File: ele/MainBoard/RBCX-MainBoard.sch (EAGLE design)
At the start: 340 parts, among them IC1 DRV8833PWP, IC10 INA180A4, IC11 AMS1117-3.3, IC2 INA180A4, IC3 INA180A4, IC4 DRV8833PWP, IC5 INA180A4, IC6 INA180A4, IC7 INA180A4, IC8 INA180A4, IC9 INA180A4, Q1 CHOOSE_ME, Q2 CHOOSE_ME, Q3 CHOOSE_ME, Q4 CHOOSE_ME, Q5 CHOOSE_ME, Q6 CHOOSE_ME, Q7 CHOOSE_ME, Q8 CHOOSE_ME, Q9 CHOOSE_ME, U1 STM32F103VCT6, X0 POWER_IN, X1 M3B, X2 M4B, X3 M3B, X4 M4B, X5 POWER_OUT, Y1 3215_2P, Y2 5032/2P

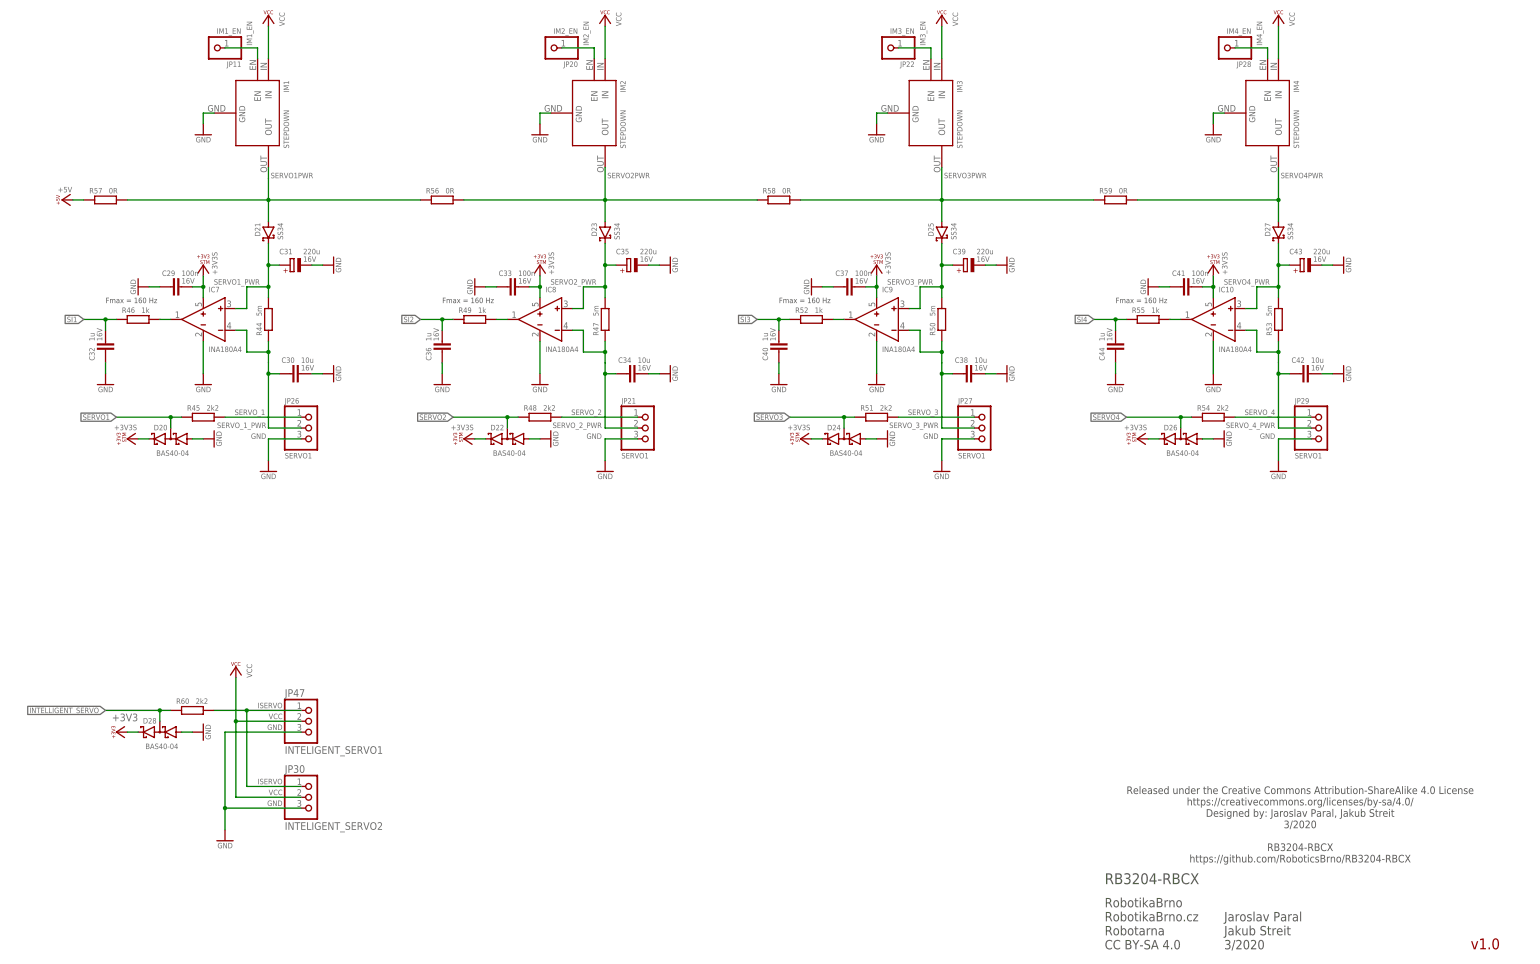
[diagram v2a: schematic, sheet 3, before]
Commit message: MainBoardSCH: Add bulk capacitor to stepdowns and drivers
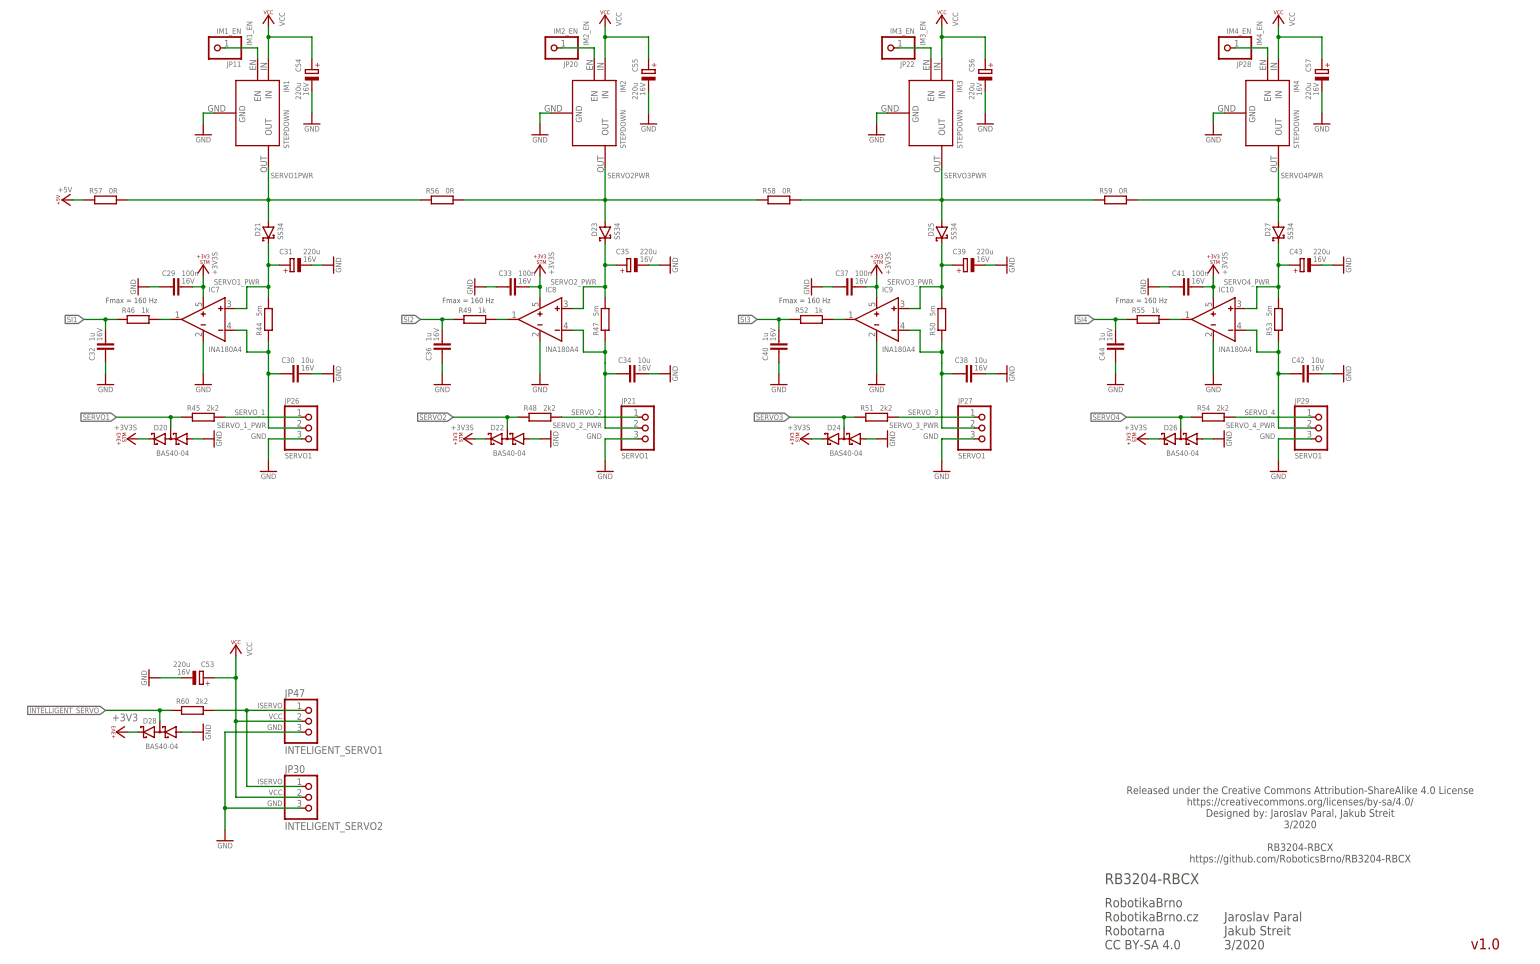
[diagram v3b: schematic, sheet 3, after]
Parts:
- added C51, C52, C53, C54, C55, C56, C57, C58: 220u, rcl_upravena:CPOL-EU153CLV-1010
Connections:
- net GND: now also C51.-, C52.-, C53.-, C54.-, C55.-, C56.-, C57.-, C58.-
- net VCC: now also C51.+, C52.+, C53.+, C54.+, C55.+, C56.+, C57.+, C58.+

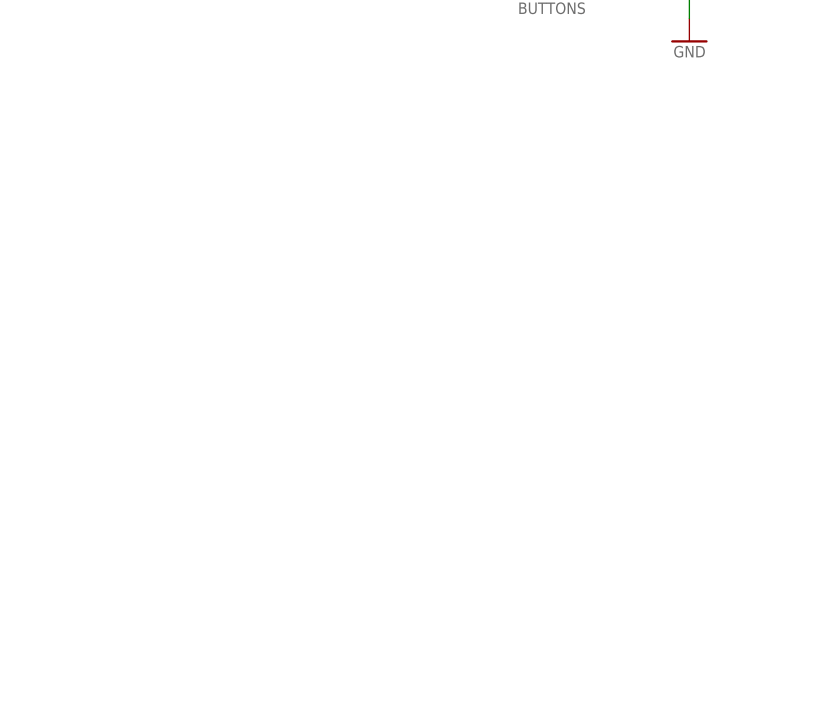
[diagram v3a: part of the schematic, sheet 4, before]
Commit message: MainBoardSCH: Add buzzer
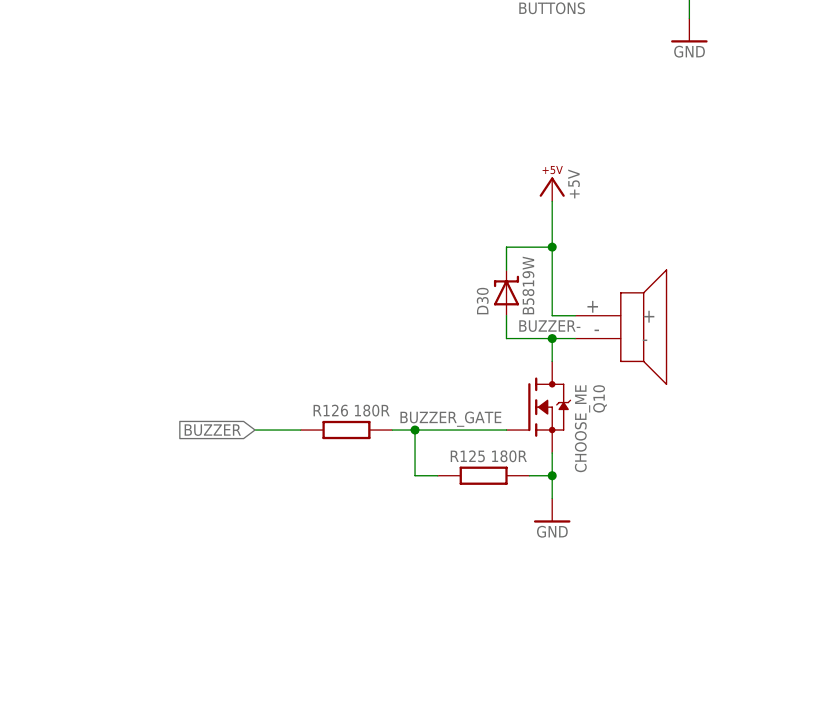
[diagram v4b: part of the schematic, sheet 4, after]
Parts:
- added D30: B5819W, diode:SHOTTKY-SOD123
- added Q10: CHOOSE_ME, transistors:N-MOSFET-SOT323-GSD
- added R125, R126: 180R, rcl_upravena:R-EU_R0603
- added U$1: PIEZO, piezo:PIEZO
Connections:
- new net BUZZER-: D30.A, Q10.D, U$1.-
- new net BUZZER_GATE: Q10.G, R125.1, R126.2
- net +5V: now also D30.C, U$1.+
- net BUZZER: now also R126.1
- net GND: now also Q10.S, R125.2
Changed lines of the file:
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@@
 </part>
 <part name="GND155" library="Supply" deviceset="GND" device=""/>
+<part name="U$1" library="piezo" deviceset="PIEZO" device=""/>
+<part name="Q10" library="transistors" deviceset="N-MOSFET" device="-SOT323-GSD" value="CHOOSE_ME"/>
+<part name="GND156" library="Supply" deviceset="GND" device=""/>
+<part name="R125" library="rcl_upravena" deviceset="R-EU_" device="R0603" value="180R"/>
+<part name="R126" library="rcl_upravena" deviceset="R-EU_" device="R0603" value="180R"/>
+<part name="P+37" library="Supply" deviceset="+5V" device=""/>
+<part name="D30" library="diode" deviceset="SHOTTKY" device="-SOD123" value="B5819W">
+<attribute name="DESCRIPTION" value="40V 1A 600mV @ 1A SOD-123 Schottky Barrier Diodes (SBD) RoHS"/>
+<attribute name="EXTENDED" value="NO"/>
+<attribute name="LCSC_ID" value="C305445"/>
+<attribute name="MF" value="Foshan Blue Rocket Elec"/>
+<attribute name="MF_ID" value="B5819W"/>
+<attribute name="PACKAGE" value="SOD-123"/>
+<attribute name="PADS" value="2"/>
+<attribute name="PRICE_100PLUS" value="$0.0176"/>
+<attribute name="PRICE_1PLUS" value="$0.0342"/>
+<attribute name="PRICE_DATE" value="17.03.2020"/>
+</part>
 </parts>
 <sheets>
@@
 <attribute name="VALUE" x="214.122" y="65.024" size="1.27" layer="96"/>
 </instance>
+<instance part="U$1" gate="G$1" x="236.22" y="142.24" smashed="yes"/>
+<instance part="Q10" gate="G$1" x="226.06" y="137.16" smashed="yes">
+<attribute name="VALUE" x="231.14" y="139.7" size="1.27" layer="96" rot="R270"/>
+<attribute name="NAME" x="233.172" y="139.7" size="1.27" layer="95" rot="R270"/>
+</instance>
+<instance part="GND156" gate="1" x="228.6" y="124.46" smashed="yes">
+<attribute name="VALUE" x="226.822" y="122.682" size="1.27" layer="96"/>
+</instance>
+<instance part="R125" gate="G$1" x="220.98" y="129.54" smashed="yes">
+<attribute name="NAME" x="217.17" y="131.064" size="1.27" layer="95"/>
+<attribute name="VALUE" x="221.742" y="131.064" size="1.27" layer="96"/>
+</instance>
+<instance part="R126" gate="G$1" x="205.74" y="134.62" smashed="yes">
+<attribute name="NAME" x="201.93" y="136.144" size="1.27" layer="95"/>
+<attribute name="VALUE" x="206.502" y="136.144" size="1.27" layer="96"/>
+</instance>
+<instance part="P+37" gate="1" x="228.6" y="162.56" smashed="yes" rot="MR0">
+<attribute name="VALUE" x="230.378" y="163.576" size="1.27" layer="96" rot="R270"/>
+</instance>
+<instance part="D30" gate="G$1" x="223.52" y="149.86" smashed="yes" rot="R90">
+<attribute name="NAME" x="221.5134" y="147.32" size="1.27" layer="95" rot="R90"/>
+<attribute name="VALUE" x="226.5934" y="147.32" size="1.27" layer="96" rot="R90"/>
+<attribute name="EXTENDED" x="223.52" y="149.86" size="1.27" layer="96" rot="R90" display="off"/>
+<attribute name="LCSC_ID" x="223.52" y="149.86" size="1.27" layer="96" rot="R90" display="off"/>
+<attribute name="MF" x="223.52" y="149.86" size="1.27" layer="96" rot="R90" display="off"/>
+<attribute name="MF_ID" x="223.52" y="149.86" size="1.27" layer="96" rot="R90" display="off"/>
+<attribute name="PACKAGE" x="223.52" y="149.86" size="1.27" layer="96" rot="R90" display="off"/>
+<attribute name="PADS" x="223.52" y="149.86" size="1.27" layer="96" rot="R90" display="off"/>
+<attribute name="PRICE_100PLUS" x="223.52" y="149.86" size="1.27" layer="96" rot="R90" display="off"/>
+<attribute name="PRICE_1PLUS" x="223.52" y="149.86" size="1.27" layer="96" rot="R90" display="off"/>
+<attribute name="PRICE_DATE" x="223.52" y="149.86" size="1.27" layer="96" rot="R90" display="off"/>
+<attribute name="DESCRIPTION" x="223.52" y="149.86" size="1.27" layer="96" rot="R90" display="off"/>
+</instance>
 </instances>
 <busses>
@@
 <junction x="243.84" y="55.88"/>
 </segment>
+<segment>
+<pinref part="Q10" gate="G$1" pin="S"/>
+<pinref part="GND156" gate="1" pin="GND"/>
+<wire x1="228.6" y1="132.08" x2="228.6" y2="129.54" width="0.1524" layer="91"/>
+<pinref part="R125" gate="G$1" pin="2"/>
+<wire x1="228.6" y1="129.54" x2="228.6" y2="127" width="0.1524" layer="91"/>
+<wire x1="226.06" y1="129.54" x2="228.6" y2="129.54" width="0.1524" layer="91"/>
+<junction x="228.6" y="129.54"/>
+</segment>
 </net>
 <net name="SERVO1" class="0">
@@
 <pinref part="U1" gate="G$1" pin="PA8"/>
 </segment>
+<segment>
+<pinref part="R126" gate="G$1" pin="1"/>
+<wire x1="200.66" y1="134.62" x2="195.58" y2="134.62" width="0.1524" layer="91"/>
+<label x="195.58" y="134.62" size="1.27" layer="95" rot="MR0" xref="yes"/>
+</segment>
 </net>
 <net name="DEBUG_TX" class="0">
@@
 </segment>
 </net>
+<net name="BUZZER-" class="0">
+<segment>
+<pinref part="U$1" gate="G$1" pin="-"/>
+<wire x1="231.14" y1="144.78" x2="228.6" y2="144.78" width="0.1524" layer="91"/>
+<pinref part="Q10" gate="G$1" pin="D"/>
+<wire x1="228.6" y1="144.78" x2="228.6" y2="142.24" width="0.1524" layer="91"/>
+<pinref part="D30" gate="G$1" pin="A"/>
+<wire x1="223.52" y1="147.32" x2="223.52" y2="144.78" width="0.1524" layer="91"/>
+<wire x1="223.52" y1="144.78" x2="228.6" y2="144.78" width="0.1524" layer="91"/>
+<junction x="228.6" y="144.78"/>
+<label x="224.79" y="145.542" size="1.27" layer="95"/>
+</segment>
+</net>
+<net name="+5V" class="0">
+<segment>
+<pinref part="U$1" gate="G$1" pin="+"/>
+<pinref part="P+37" gate="1" pin="+5V"/>
+<wire x1="231.14" y1="147.32" x2="228.6" y2="147.32" width="0.1524" layer="91"/>
+<wire x1="228.6" y1="147.32" x2="228.6" y2="154.94" width="0.1524" layer="91"/>
+<pinref part="D30" gate="G$1" pin="C"/>
+<wire x1="228.6" y1="154.94" x2="228.6" y2="160.02" width="0.1524" layer="91"/>
+<wire x1="223.52" y1="152.4" x2="223.52" y2="154.94" width="0.1524" layer="91"/>
+<wire x1="223.52" y1="154.94" x2="228.6" y2="154.94" width="0.1524" layer="91"/>
+<junction x="228.6" y="154.94"/>
+</segment>
+</net>
+<net name="BUZZER_GATE" class="0">
+<segment>
+<pinref part="R126" gate="G$1" pin="2"/>
+<pinref part="Q10" gate="G$1" pin="G"/>
+<wire x1="210.82" y1="134.62" x2="213.36" y2="134.62" width="0.1524" layer="91"/>
+<pinref part="R125" gate="G$1" pin="1"/>
+<wire x1="213.36" y1="134.62" x2="223.52" y2="134.62" width="0.1524" layer="91"/>
+<wire x1="215.9" y1="129.54" x2="213.36" y2="129.54" width="0.1524" layer="91"/>
+<wire x1="213.36" y1="129.54" x2="213.36" y2="134.62" width="0.1524" layer="91"/>
+<junction x="213.36" y="134.62"/>
+<label x="211.582" y="135.382" size="1.27" layer="95"/>
+</segment>
+</net>
